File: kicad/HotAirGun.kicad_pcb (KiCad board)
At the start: 2 copper layers, 65 parts, among them J1 CONN_02X03, J10 CONN_01X06, J2 CONN_01X06, J3 CONN_02X02, J4 HAG Resistor, J5 PWR_IN, J6 PWR_Suply, J7 Vin, J8 Foot Switch, J9 CONN_01X06, Q1 Q_NPN_CBE, Q2 Q_PNP_CBE, Q3 IRF740, SW1 Start, SW2 Stop, SW3 WeldCurv, SW4 Rotary_Encoder_Switch_V2, U1 MCP23017, U2 MOC3023M, U3 LM2575, U4 MAX6675

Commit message: New PCB version with smd component Added plot folder with gerber file
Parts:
- added ?: Choke_SMD_PISR_Handsoldering_FASTRON, Choke_SMD:Choke_SMD_PISR_Handsoldering_FASTRON, F.Cu at (126.0, 127.9)
- added G***: LOGO, Msystem:LOGO, B.Cu at (209.6, 106.4)
- added G***: LOGO, Msystem:LOGO, F.Cu at (209.6, 106.7)
- added G***: LOGO, Msystem:LOGO, F.Cu at (94.5, 115.3)
- added REF**: , Mounting_Holes:MountingHole_3.2mm_M3, F.Cu at (155.2, 61.2)
- added REF**: , Mounting_Holes:MountingHole_3.2mm_M3, F.Cu at (58.7, 61.2)
- added REF**: , Mounting_Holes:MountingHole_3.2mm_M3, F.Cu at (58.7, 133.6)
- added REF**: , Mounting_Holes:MountingHole_3.2mm_M3, F.Cu at (155.2, 133.6)
- added REF**: , Mounting_Holes:MountingHole_3.2mm_M3, F.Cu at (217.4, 76.5)
- added REF**: , Mounting_Holes:MountingHole_3.2mm_M3, F.Cu at (217.4, 115.8)
- Arduino Nano: renamed from XA1
- C3, C4, R13, R15, R16, R17, R19, R20, R7, R8, R9, U4: moved to F.Cu
- D2, J1, J2, J3: moved to B.Cu
- F2: value Fuse -> Polyfuse_Small; footprint Fuse_Holders_and_Fuses:Fuseholder5x20_horiz_open_Schurter_0031_8201 -> Fuse_Holders_and_Fuses:Fuse_TE5_Littlefuse-395Series
- J8: footprint Connect:JACK_ALIM -> Connectors_Molex:Molex_KK-6410-02_02x2.54mm_Straight
- R1: footprint Discret:R3 -> Resistors_SMD:R_0603; moved to B.Cu
- R11, R14: footprint Resistors_ThroughHole:Resistor_Horizontal_RM10mm -> Resistors_SMD:R_0603_HandSoldering
- R18: footprint Resistors_ThroughHole:Resistor_Horizontal_RM7mm -> Resistors_SMD:R_0603_HandSoldering; moved to F.Cu
- moved J8 118.7 mm to (153.7, 109.5), turned to 90 degrees
- moved D7 115.5 mm to (151.1, 126.0), turned to 90 degrees
- moved R16 108.4 mm to (151.1, 118.6), turned to 270 degrees
- moved C2 100.0 mm to (141.6, 123.4), turned to 270 degrees
- moved U3 97.0 mm to (109.9, 134.2), turned to 180 degrees
- moved L2 95.0 mm to (125.7, 127.9), turned to 90 degrees
- moved Q1 89.8 mm to (168.9, 83.4), turned to 90 degrees
- moved J7 88.4 mm to (68.6, 126.0), turned to 270 degrees
- moved D8 85.1 mm to (152.4, 93.0), turned to 270 degrees
- moved DS1 84.8 mm to (167.6, 129.8), turned to 90 degrees
- moved D9 83.8 mm to (113.7, 126.0), turned to 180 degrees
- moved R19 82.9 mm to (109.9, 120.3), turned to 180 degrees
- moved C1 81.4 mm to (87.0, 124.7), turned to 270 degrees
- moved R1 80.3 mm to (174.1, 82.8), turned to 0 degrees
- moved R20 80.2 mm to (109.9, 118.4), turned to 0 degrees
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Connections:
- F2 pad 1: 220F -> +24V
- J6 pad 1: Net-(F2-Pad2) -> 220F
- J7 pad 1: +24V -> Net-(F2-Pad2)
- R4 pad 1: Net-(J1-Pad2) -> Net-(J1-Pad6)
- R6 pad 1: Net-(J1-Pad6) -> Net-(J1-Pad2)
- SW4 pad S1: Net-(SW4-PadS1) -> Gnd_P
- SW4 pad S2: Gnd_P -> Net-(SW4-PadS2)
- U1 pad 15: Net-(J1-Pad2) -> Net-(J1-Pad6)
- U1 pad 17: Net-(J1-Pad6) -> Net-(J1-Pad2)
- U1 pad 21: Net-(SW4-PadS1) -> Net-(SW4-PadS2)
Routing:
- net FOOT_SW: track 111.8 -> 29.0 mm, vias 2 -> 0
- net Gnd_P: track 379.3 -> 304.6 mm, vias 4 -> 2
- net Net-(SW4-PadS1): track 66.9 -> 0.00 mm
- net Earth: track 433.1 -> 369.2 mm, vias 4 -> 0
- net Vcc_P: track 208.7 -> 154.5 mm, vias 2 -> 0
- net Net-(SW4-PadS2): track 0.00 -> 50.6 mm
- net TILT: track 76.5 -> 38.6 mm, vias 2 -> 0
- net FAN: track 70.7 -> 39.3 mm, vias 0 -> 2
- net +24V: track 111.5 -> 136.2 mm, vias 2 -> 0
- net 220F: track 51.9 -> 75.0 mm
- net Net-(C3-Pad2): track 5.62 -> 27.0 mm
- net SO: track 51.9 -> 34.9 mm
- net 220N: track 78.5 -> 62.7 mm
- net Buz: track 8.85 -> 24.5 mm
- net Net-(DS1-Pad3): track 23.2 -> 7.78 mm
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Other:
- board outline added: 176 x 82.5 mm
- board text added: "CtrlPanel V1.0 3Key"
- board text added: "HotAirGun V2.0"

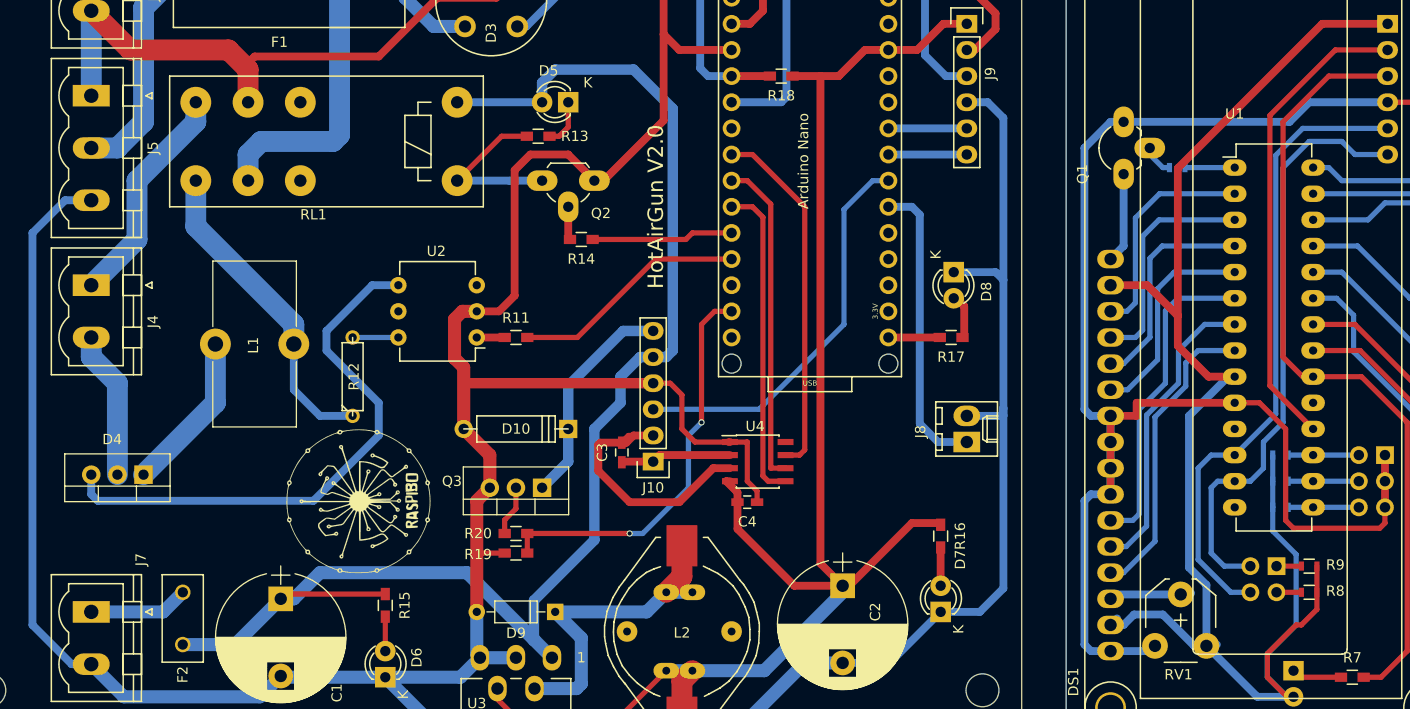
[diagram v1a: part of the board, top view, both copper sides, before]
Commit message: Update with new PCB version
Kicad schematic and pcb layout correction on Mosfet and Triac footprint.
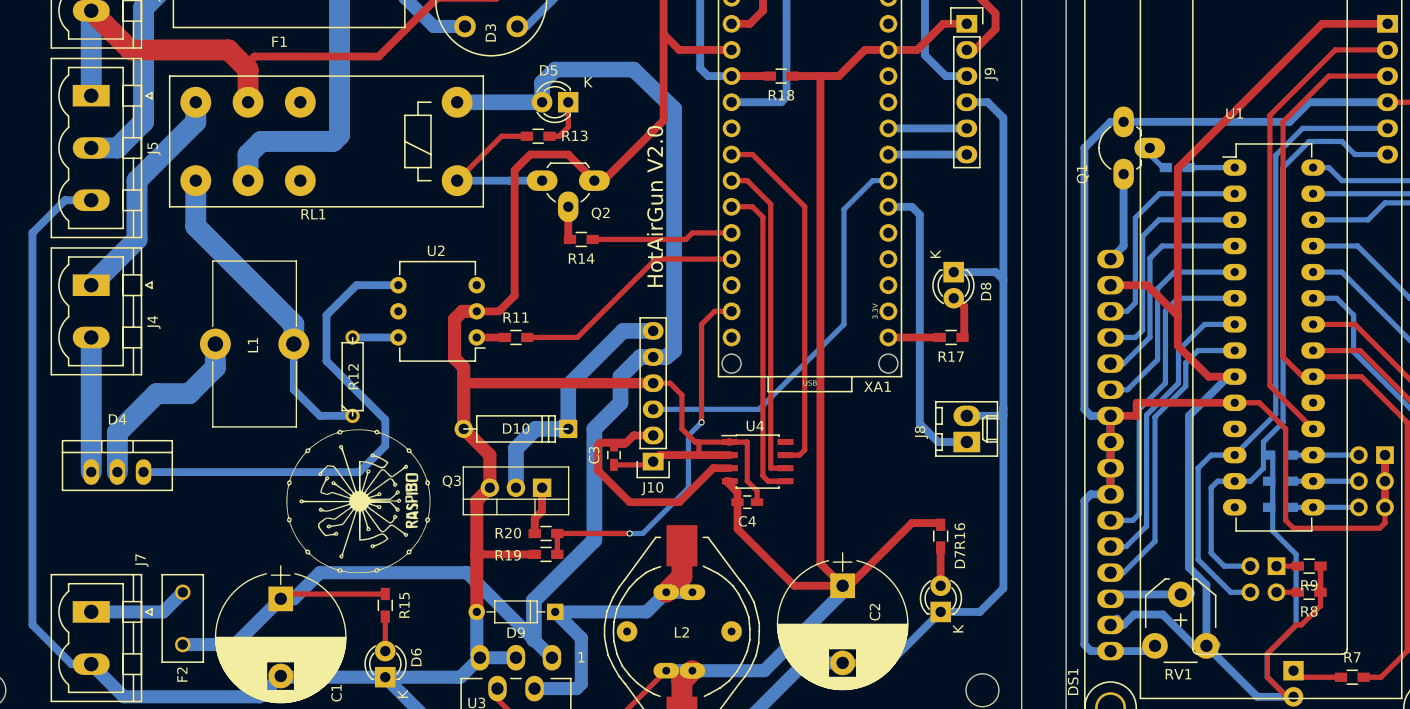
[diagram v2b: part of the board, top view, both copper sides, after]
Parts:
- removed Arduino Nano: Arduino_Nano_Socket, Arduino:Arduino_Nano_Socket
- added XA1: Arduino_Nano_Socket, Arduino:Arduino_Nano_Socket, F.Cu at (138.4, 103.1)
- C1: value CP -> 100uF
- C2: value CP -> 470uF
- D4: footprint TO_SOT_Packages_THT:TO-220_Vertical -> TO_SOT_Packages_THT:TO-220_Neutral123_Vertical
- R1, R4, R5, R6, R8, R9: footprint Resistors_SMD:R_0603 -> Resistors_SMD:R_0603_HandSoldering
- R10: value 56k -> 100k
- R18: value 15K -> 12K
- RV1: value POT -> 10K
- moved R19 2.92 mm to (112.8, 120.4)
- moved R20 2.92 mm to (112.8, 118.4)
- moved D4 2.55 mm to (71.1, 112.4), turned to 0 degrees
- moved C3 0.80 mm to (119.4, 110.7)
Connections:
- C3 pad 1: Net-(C3-Pad1) -> Earth
- J10 pad 1: Net-(C3-Pad1) -> Earth
- J10 pad 3: TILT -> S_SW
- J4 pad 2: Net-(D4-Pad2) -> Net-(D4-Pad1)
- L1 pad 2: Net-(D4-Pad1) -> Net-(D4-Pad2)
- Q3 pad 1: Net-(D10-Pad1) -> Net-(Q3-Pad1)
- Q3 pad 2: Net-(Q3-Pad2) -> Net-(D10-Pad1)
- R20 pad 1: Net-(Q3-Pad2) -> Net-(Q3-Pad1)
- U4 pad 2: Net-(C3-Pad1) -> Earth
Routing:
- net TILT: track 38.6 -> 0.00 mm
- net S_SW: track 0.00 -> 38.6 mm
- net Earth: track 369.2 -> 381.5 mm
- net Net-(C3-Pad1): track 10.8 -> 0.00 mm
- net Net-(D4-Pad3): track 53.8 -> 47.8 mm
- net Net-(Q3-Pad2): track 4.90 -> 0.00 mm
- net Net-(Q3-Pad1): track 0.00 -> 4.74 mm
- net Net-(D4-Pad2): track 14.4 -> 18.3 mm
- net Net-(D10-Pad1): track 21.4 -> 24.3 mm
- net FAN: track 39.3 -> 36.5 mm
- net Vcc_P: track 154.5 -> 157.2 mm
- net Net-(D4-Pad1): track 15.6 -> 13.1 mm

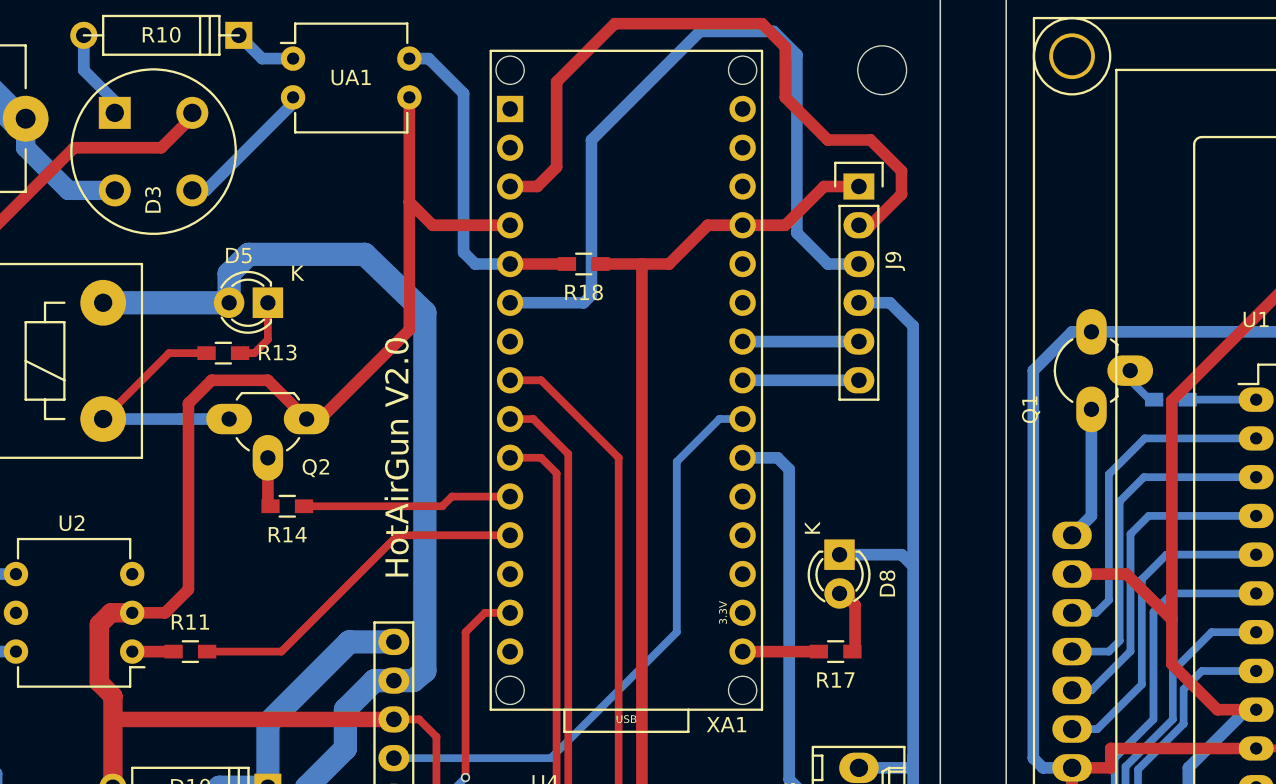
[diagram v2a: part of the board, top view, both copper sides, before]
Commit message: Kicad project  mistake correction
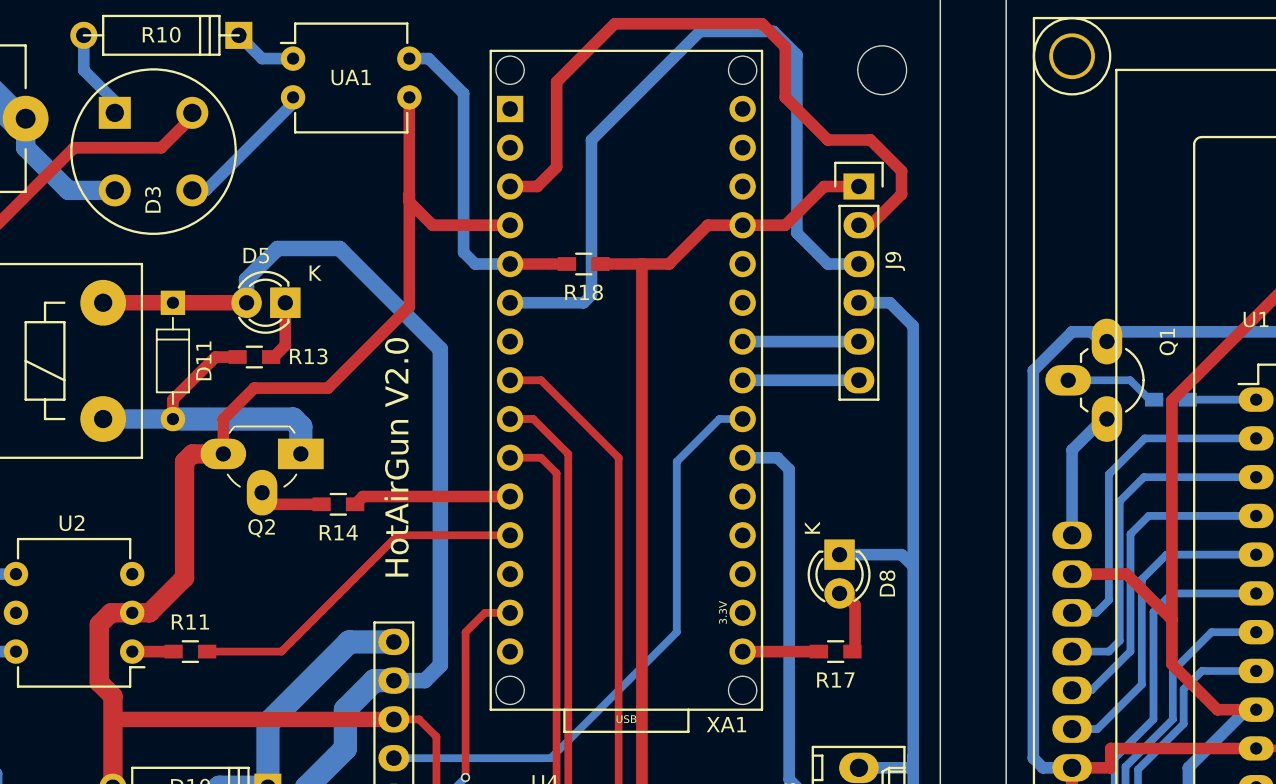
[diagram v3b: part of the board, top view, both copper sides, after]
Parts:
- added D11: 1N4007, Diodes_THT:D_DO-35_SOD27_P7.62mm_Horizontal, F.Cu at (108.7, 76.5)
- moved Q1 4.56 mm to (169.9, 79.0), turned to 270 degrees
- moved R14 3.35 mm to (119.5, 89.7)
- moved Q2 2.32 mm to (117.1, 86.4)
- moved R13 2.05 mm to (114.0, 80.0)
- moved D5 1.14 mm to (116.1, 76.5)
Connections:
- Q1 pad 1: Net-(DS1-Pad16) -> Gnd_P
- Q1 pad 3: Gnd_P -> Net-(DS1-Pad16)
- Q2 pad 1: Earth -> Net-(D11-Pad2)
- Q2 pad 3: Net-(Q2-Pad3) -> Earth
- R13 pad 2: Net-(Q2-Pad3) -> Net-(D11-Pad2)
- RL1 pad A1: Net-(Q2-Pad3) -> Net-(D11-Pad2)
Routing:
- net Net-(D11-Pad2): track 0.00 -> 21.6 mm
- net Net-(Q2-Pad3): track 16.8 -> 0.00 mm
- net +24V: track 136.4 -> 141.5 mm
- net Earth: track 381.5 -> 377.6 mm
- net Net-(Q1-Pad2): track 3.08 -> 6.51 mm
- net SAFE_REL: track 13.8 -> 10.4 mm
- net Gnd_P: track 304.6 -> 305.8 mm
- net Net-(Q2-Pad2): track 3.25 -> 4.21 mm
- net Net-(D5-Pad1): track 4.60 -> 4.04 mm

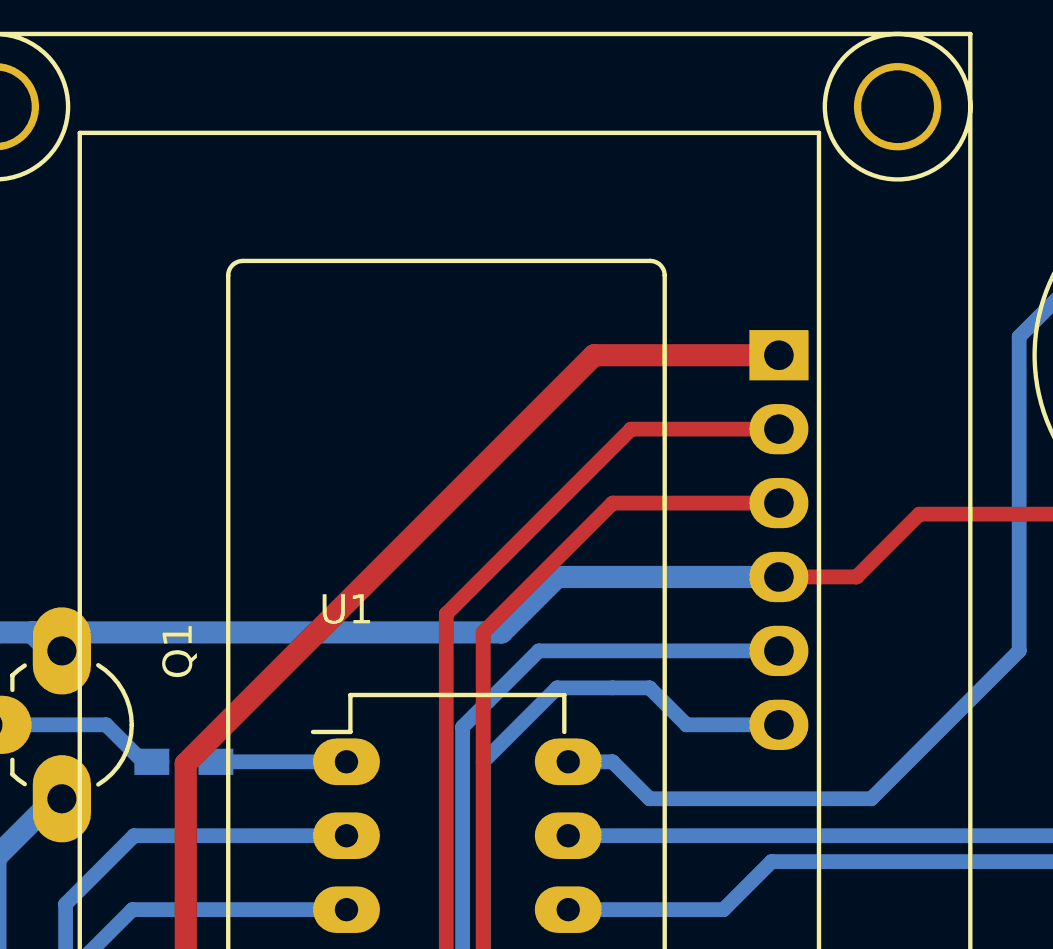
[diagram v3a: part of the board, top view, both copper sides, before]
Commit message: Added C5 bypass capacitor
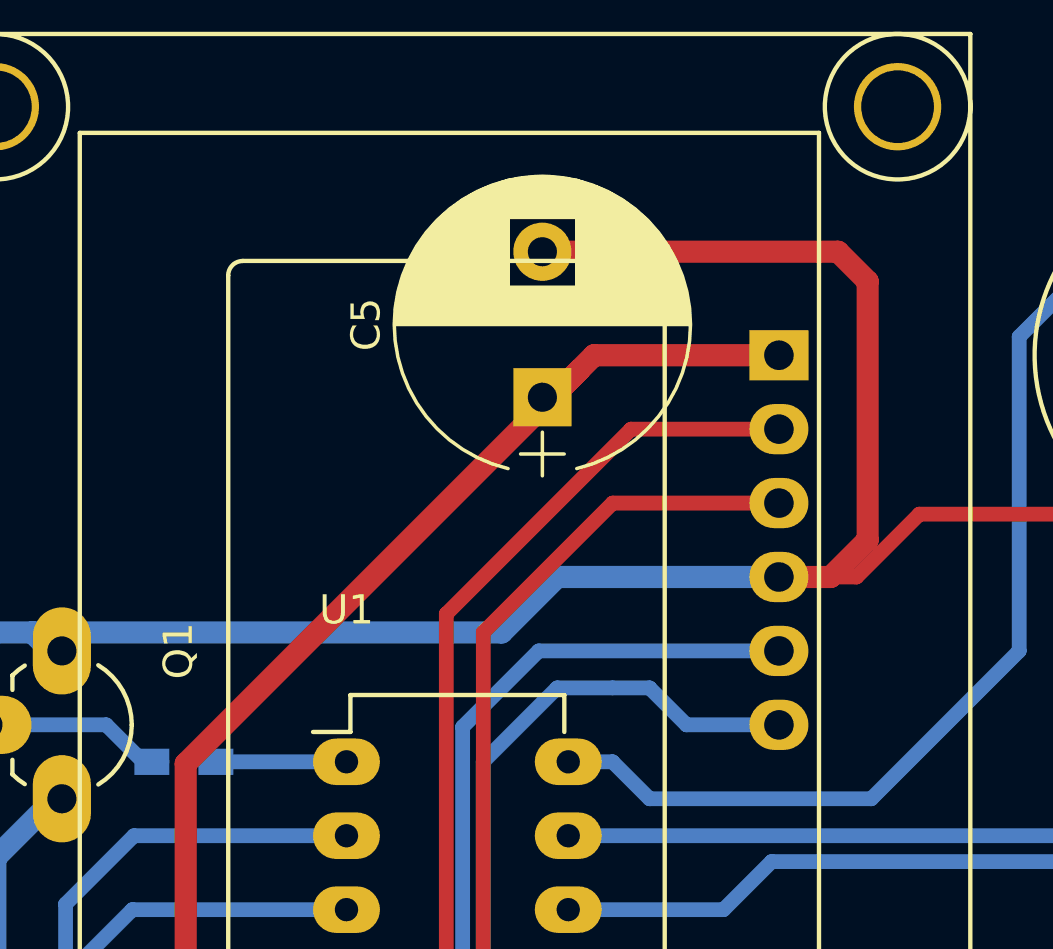
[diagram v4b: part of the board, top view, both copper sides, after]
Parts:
- added C5: 10uF, Capacitors_THT:CP_Radial_D10.0mm_P5.00mm, F.Cu at (186.4, 70.3)
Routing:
- net Gnd_P: track 305.8 -> 329.9 mm
- net Vcc_P: track 157.2 -> 158.9 mm
